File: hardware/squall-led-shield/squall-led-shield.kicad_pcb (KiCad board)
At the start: 2 copper layers, 25.4 x 21 mm, 10 parts, among them J1 SQUALL_HEADER, Q1 Q_2NMOS

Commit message: WIP: Okay, the router is cool once you get it
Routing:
- net Net-(J1-Pad16): track 0.00 -> 7.65 mm, vias 0 -> 1
- net Net-(J1-Pad14): track 0.00 -> 7.39 mm, vias 0 -> 1
- net Net-(J1-Pad18): track 0.00 -> 4.70 mm, vias 0 -> 1
- net Net-(J1-Pad19): track 0.00 -> 4.39 mm, vias 0 -> 1
- net Net-(J1-Pad12): track 0.00 -> 4.33 mm, vias 0 -> 1
- net Net-(J1-Pad20): track 0.00 -> 3.77 mm, vias 0 -> 1
- net Net-(J1-Pad13): track 0.00 -> 3.43 mm, vias 0 -> 1
- net Net-(J1-Pad11): track 0.00 -> 3.04 mm, vias 0 -> 1
- net Net-(J1-Pad15): track 0.00 -> 2.96 mm, vias 0 -> 1
- net Net-(J1-Pad17): track 0.00 -> 2.52 mm, vias 0 -> 1
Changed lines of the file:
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@@
     (thickness 1.6)
     (drawings 3)
-    (tracks 70)
+    (tracks 150)
     (zones 0)
     (modules 10)
@@
   (via (at 145.288 100.457) (size 0.8128) (drill 0.4064) (layers F.Cu B.Cu) (net 12))
   (segment (start 144.23 99.46) (end 144.799 99.46) (width 0.2032) (layer F.Cu) (net 12))
+  (segment (start 161.390368 102.472047) (end 161.390368 103.052832) (width 0.2032) (layer B.Cu) (net 13))
+  (segment (start 161.390368 103.052832) (end 161.1032 103.34) (width 0.2032) (layer B.Cu) (net 13))
+  (segment (start 161.1032 103.34) (end 160.57 103.34) (width 0.2032) (layer B.Cu) (net 13))
+  (segment (start 160.57 103.34) (end 161.1032 103.34) (width 0.2032) (layer F.Cu) (net 13))
+  (segment (start 161.1032 103.34) (end 161.390368 103.052832) (width 0.2032) (layer F.Cu) (net 13))
+  (segment (start 161.390368 103.052832) (end 161.390368 102.472047) (width 0.2032) (layer F.Cu) (net 13))
+  (via (at 161.390368 102.472047) (size 0.8128) (drill 0.4064) (layers F.Cu B.Cu) (net 13))
+  (segment (start 163.28 103.34) (end 163.767202 103.34) (width 0.2032) (layer B.Cu) (net 14))
+  (segment (start 163.522198 102.181198) (end 163.195 102.181198) (width 0.2032) (layer B.Cu) (net 14))
+  (segment (start 163.767202 103.34) (end 163.864001 103.243201) (width 0.2032) (layer B.Cu) (net 14))
+  (segment (start 163.864001 103.243201) (end 163.864001 102.523001) (width 0.2032) (layer B.Cu) (net 14))
+  (segment (start 163.864001 102.523001) (end 163.522198 102.181198) (width 0.2032) (layer B.Cu) (net 14))
+  (segment (start 163.28 103.34) (end 163.8132 103.34) (width 0.2032) (layer F.Cu) (net 14))
+  (segment (start 163.8132 103.34) (end 163.864001 103.289199) (width 0.2032) (layer F.Cu) (net 14))
+  (segment (start 163.864001 103.289199) (end 163.864001 102.536799) (width 0.2032) (layer F.Cu) (net 14))
+  (segment (start 163.864001 102.536799) (end 163.5084 102.181198) (width 0.2032) (layer F.Cu) (net 14))
+  (segment (start 163.5084 102.181198) (end 163.195 102.181198) (width 0.2032) (layer F.Cu) (net 14))
+  (via (at 163.195 102.181198) (size 0.8128) (drill 0.4064) (layers F.Cu B.Cu) (net 14))
+  (segment (start 162.052 103.174797) (end 161.486797 103.74) (width 0.2032) (layer F.Cu) (net 15))
+  (segment (start 161.486797 103.74) (end 160.57 103.74) (width 0.2032) (layer F.Cu) (net 15))
+  (segment (start 160.57 103.74) (end 161.486797 103.74) (width 0.2032) (layer B.Cu) (net 15))
+  (segment (start 161.486797 103.74) (end 162.052 103.174797) (width 0.2032) (layer B.Cu) (net 15))
+  (via (at 162.052 103.174797) (size 0.8128) (drill 0.4064) (layers F.Cu B.Cu) (net 15))
+  (segment (start 163.195 101.215995) (end 164.21961 102.240605) (width 0.2032) (layer F.Cu) (net 16))
+  (segment (start 164.21961 102.240605) (end 164.21961 103.436498) (width 0.2032) (layer F.Cu) (net 16))
+  (segment (start 164.21961 103.436498) (end 163.916108 103.74) (width 0.2032) (layer F.Cu) (net 16))
+  (segment (start 163.916108 103.74) (end 163.8132 103.74) (width 0.2032) (layer F.Cu) (net 16))
+  (segment (start 163.8132 103.74) (end 163.28 103.74) (width 0.2032) (layer F.Cu) (net 16))
+  (segment (start 163.28 103.74) (end 163.87011 103.74) (width 0.2032) (layer B.Cu) (net 16))
+  (segment (start 163.87011 103.74) (end 164.219611 103.390499) (width 0.2032) (layer B.Cu) (net 16))
+  (segment (start 164.219611 103.390499) (end 164.219611 102.240606) (width 0.2032) (layer B.Cu) (net 16))
+  (segment (start 164.219611 102.240606) (end 163.195 101.215995) (width 0.2032) (layer B.Cu) (net 16))
+  (via (at 163.195 101.215995) (size 0.8128) (drill 0.4064) (layers F.Cu B.Cu) (net 16))
+  (segment (start 162.052 104.14) (end 160.57 104.14) (width 0.2032) (layer B.Cu) (net 17))
+  (segment (start 160.57 104.14) (end 162.052 104.14) (width 0.2032) (layer F.Cu) (net 17))
+  (via (at 162.052 104.14) (size 0.8128) (drill 0.4064) (layers F.Cu B.Cu) (net 17))
+  (segment (start 164.298476 101.385524) (end 164.575221 101.662269) (width 0.2032) (layer B.Cu) (net 18))
+  (segment (start 164.575221 101.662269) (end 164.575221 103.537797) (width 0.2032) (layer B.Cu) (net 18))
+  (segment (start 164.575221 103.537797) (end 164.004017 104.109001) (width 0.2032) (layer B.Cu) (net 18))
+  (segment (start 164.004017 104.109001) (end 163.310999 104.109001) (width 0.2032) (layer B.Cu) (net 18))
+  (segment (start 163.310999 104.109001) (end 163.28 104.14) (width 0.2032) (layer B.Cu) (net 18))
+  (segment (start 163.28 104.14) (end 164.019016 104.14) (width 0.2032) (layer F.Cu) (net 18))
+  (segment (start 164.019016 104.14) (end 164.57522 103.583796) (width 0.2032) (layer F.Cu) (net 18))
+  (segment (start 164.57522 103.583796) (end 164.57522 101.662268) (width 0.2032) (layer F.Cu) (net 18))
+  (segment (start 164.57522 101.662268) (end 164.298476 101.385524) (width 0.2032) (layer F.Cu) (net 18))
+  (via (at 164.298476 101.385524) (size 0.8128) (drill 0.4064) (layers F.Cu B.Cu) (net 18))
+  (segment (start 161.454603 105.123367) (end 161.454603 104.891403) (width 0.2032) (layer B.Cu) (net 19))
+  (segment (start 161.454603 104.891403) (end 161.1032 104.54) (width 0.2032) (layer B.Cu) (net 19))
+  (segment (start 161.1032 104.54) (end 160.57 104.54) (width 0.2032) (layer B.Cu) (net 19))
+  (segment (start 160.57 104.54) (end 161.1032 104.54) (width 0.2032) (layer F.Cu) (net 19))
+  (segment (start 161.1032 104.54) (end 161.454603 104.891403) (width 0.2032) (layer F.Cu) (net 19))
+  (segment (start 161.454603 104.891403) (end 161.454603 105.123367) (width 0.2032) (layer F.Cu) (net 19))
+  (via (at 161.454603 105.123367) (size 0.8128) (drill 0.4064) (layers F.Cu B.Cu) (net 19))
+  (segment (start 162.306 106.172) (end 162.306 104.9808) (width 0.2032) (layer B.Cu) (net 20))
+  (segment (start 162.306 104.9808) (end 162.7468 104.54) (width 0.2032) (layer B.Cu) (net 20))
+  (segment (start 162.7468 104.54) (end 163.28 104.54) (width 0.2032) (layer B.Cu) (net 20))
+  (segment (start 163.28 104.54) (end 162.7468 104.54) (width 0.2032) (layer F.Cu) (net 20))
+  (segment (start 162.7468 104.54) (end 162.306 104.9808) (width 0.2032) (layer F.Cu) (net 20))
+  (segment (start 162.306 104.9808) (end 162.306 106.172) (width 0.2032) (layer F.Cu) (net 20))
+  (via (at 162.306 106.172) (size 0.8128) (drill 0.4064) (layers F.Cu B.Cu) (net 20))
+  (segment (start 160.57 104.94) (end 160.082798 104.94) (width 0.2032) (layer F.Cu) (net 21))
+  (segment (start 160.082798 104.94) (end 159.985999 105.036799) (width 0.2032) (layer F.Cu) (net 21))
+  (segment (start 159.985999 105.036799) (end 159.985999 105.756999) (width 0.2032) (layer F.Cu) (net 21))
+  (segment (start 159.985999 105.756999) (end 160.401 106.172) (width 0.2032) (layer F.Cu) (net 21))
+  (segment (start 160.401 106.172) (end 160.655 106.172) (width 0.2032) (layer F.Cu) (net 21))
+  (segment (start 160.57 104.94) (end 160.0368 104.94) (width 0.2032) (layer B.Cu) (net 21))
+  (segment (start 160.0368 104.94) (end 159.985999 104.990801) (width 0.2032) (layer B.Cu) (net 21))
+  (segment (start 159.985999 104.990801) (end 159.985999 105.743201) (width 0.2032) (layer B.Cu) (net 21))
+  (segment (start 159.985999 105.743201) (end 160.414798 106.172) (width 0.2032) (layer B.Cu) (net 21))
+  (segment (start 160.414798 106.172) (end 160.655 106.172) (width 0.2032) (layer B.Cu) (net 21))
+  (via (at 160.655 106.172) (size 0.8128) (drill 0.4064) (layers F.Cu B.Cu) (net 21))
+  (segment (start 163.449 106.098802) (end 163.864001 105.683801) (width 0.2032) (layer F.Cu) (net 22))
+  (segment (start 163.864001 105.683801) (end 163.864001 104.990801) (width 0.2032) (layer F.Cu) (net 22))
+  (segment (start 163.864001 104.990801) (end 163.8132 104.94) (width 0.2032) (layer F.Cu) (net 22))
+  (segment (start 163.8132 104.94) (end 163.28 104.94) (width 0.2032) (layer F.Cu) (net 22))
+  (segment (start 163.28 104.94) (end 163.8132 104.94) (width 0.2032) (layer B.Cu) (net 22))
+  (segment (start 163.8132 104.94) (end 163.864001 104.990801) (width 0.2032) (layer B.Cu) (net 22))
+  (segment (start 163.864001 104.990801) (end 163.864001 105.683801) (width 0.2032) (layer B.Cu) (net 22))
+  (segment (start 163.864001 105.683801) (end 163.449 106.098802) (width 0.2032) (layer B.Cu) (net 22))
+  (via (at 163.449 106.098802) (size 0.8128) (drill 0.4064) (layers F.Cu B.Cu) (net 22))
   (segment (start 151.468 94.912) (end 151.743 94.637) (width 0.2032) (layer F.Cu) (net 23))
   (segment (start 151.743 94.637) (end 153.67 94.637) (width 0.2032) (layer F.Cu) (net 23))

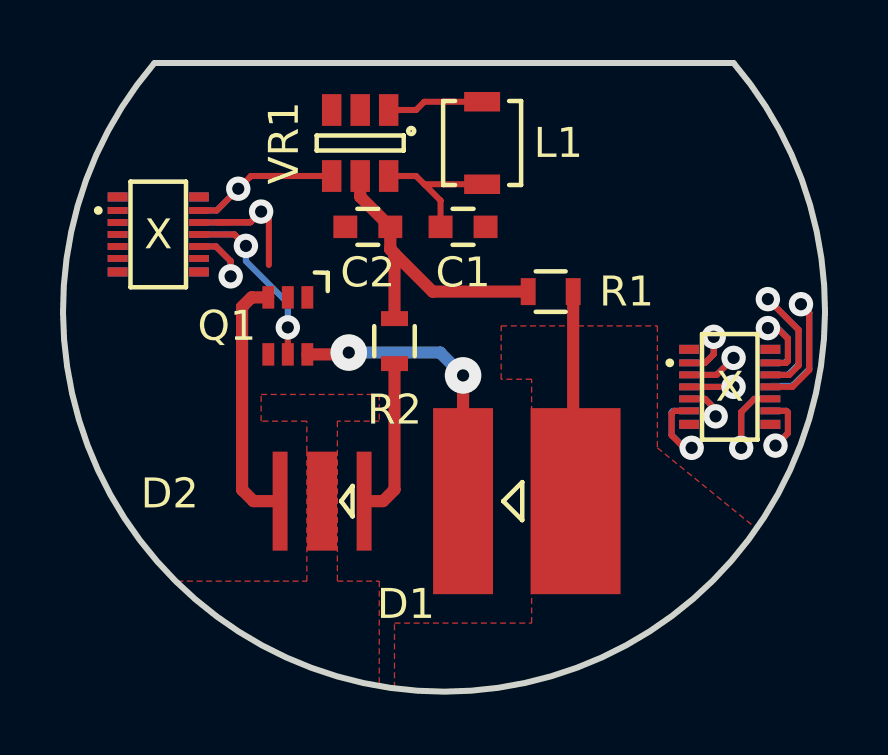
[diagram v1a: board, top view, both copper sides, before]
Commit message: WIP: Tie regulator to VCC
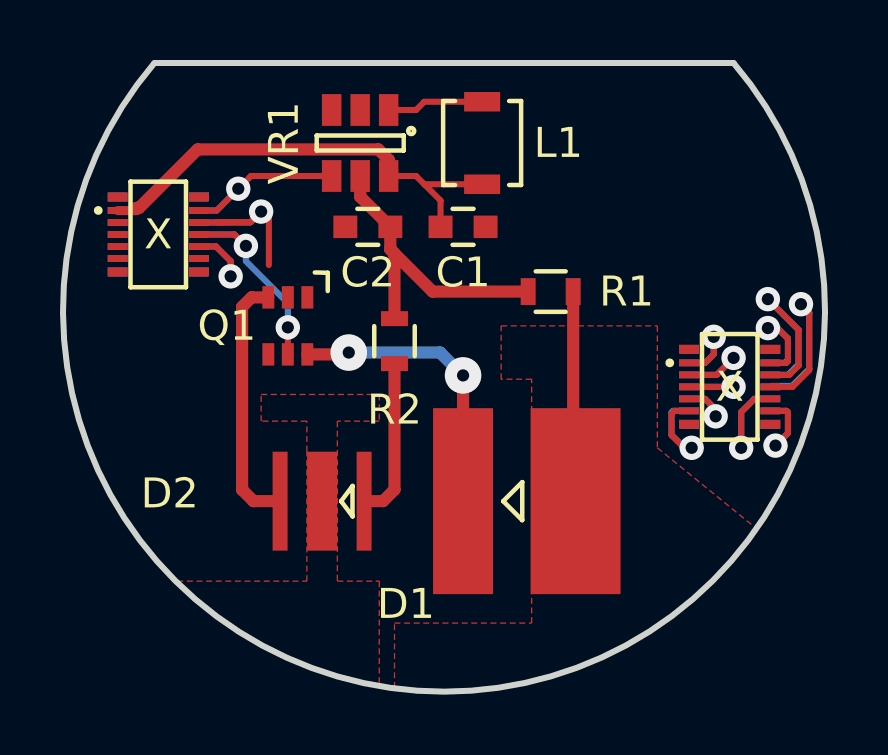
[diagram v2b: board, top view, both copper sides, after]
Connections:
- C1 pad 1: Net-(C1-Pad1) -> VCC
- L1 pad 1: Net-(C1-Pad1) -> VCC
- VR1 pad 6: Net-(C1-Pad1) -> VCC
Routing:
- net VCC: track 0.00 -> 16.3 mm
- net Net-(C1-Pad1): track 4.98 -> 0.00 mm

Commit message: Okay. That may be a board. Finally.
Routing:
- net GND: track 0.00 -> 13.5 mm, vias 0 -> 7
- net /CREE_THERMAL: track 0.00 -> 9.54 mm, vias 0 -> 3
- net Net-(D1-Pad2): track 7.02 -> 16.5 mm, vias 0 -> 3
- net /LED_IR: track 7.31 -> 8.65 mm
- added copper zone on B.Cu, net /CREE_THERMAL
- added copper zone on B.Cu, net GND
- added copper zone on F.Cu, net GND
- added copper zone on B.Cu, net Net-(D1-Pad2)

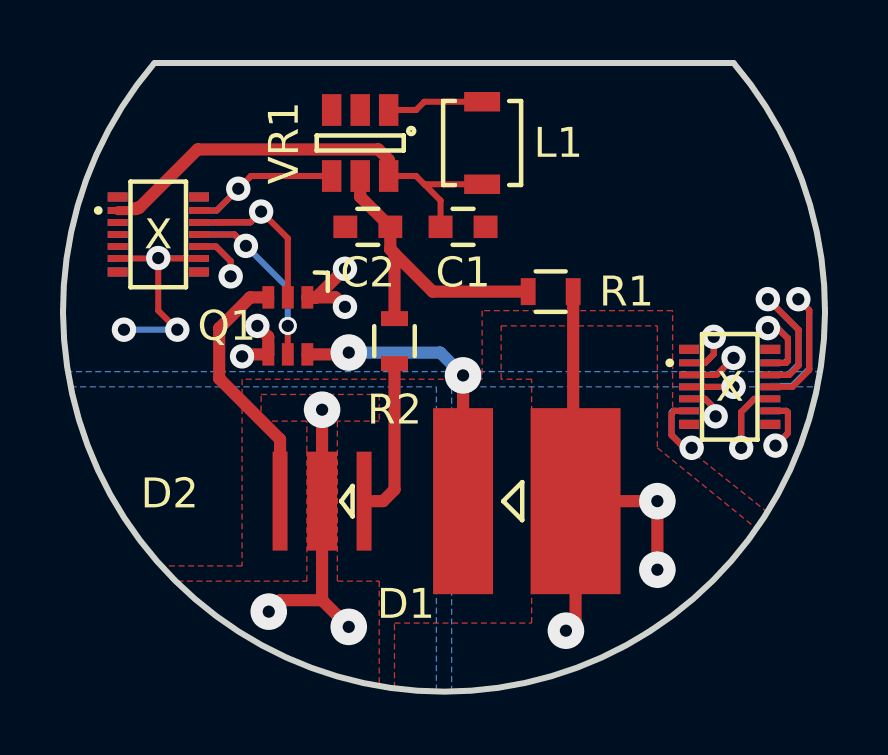
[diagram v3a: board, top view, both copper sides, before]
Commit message: Clean up silkscreen
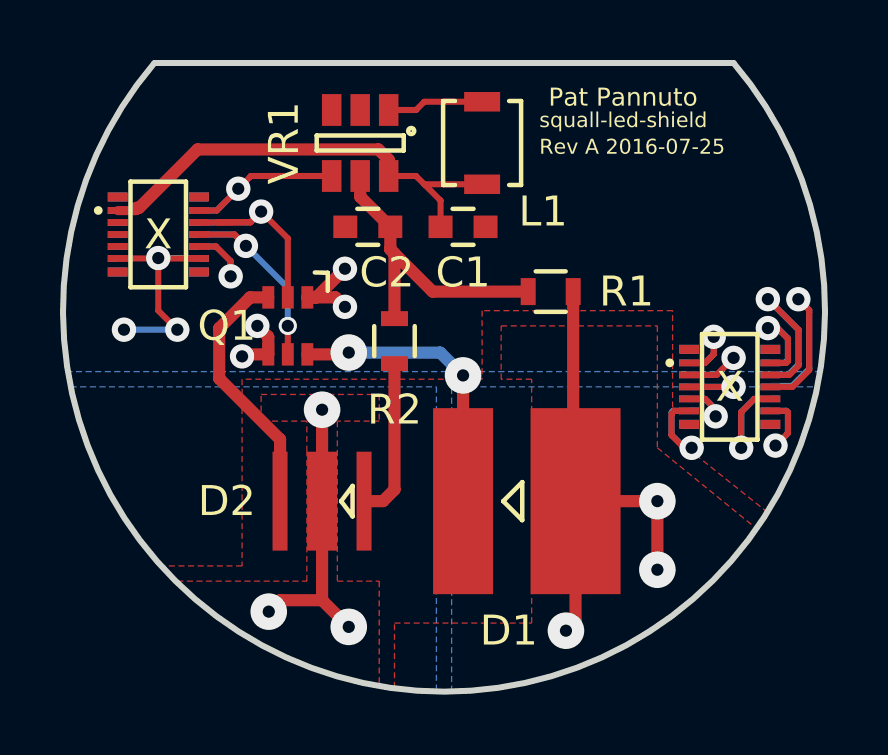
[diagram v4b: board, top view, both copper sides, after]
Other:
- board text added: "Pat Pannuto"
- board text added: "Rev A 2016-07-25"
- board text added: "squall-led-shield"
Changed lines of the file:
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@@
   (general
     (links 41)
-    (no_connects 7)
+    (no_connects 11)
     (area 137.2318 92.590943 282.218715 163.828)
     (thickness 1.6)
-    (drawings 3)
+    (drawings 6)
     (tracks 199)
     (zones 0)
@@
     (uvia_min_drill 0.1524)
     (pcb_text_width 0.3)
-    (pcb_text_size 1.5 1.5)
+    (pcb_text_size 1.016 1.016)
     (mod_edge_width 0.15)
     (mod_text_size 1 1)
@@
     (tags "capacitor 0603")
     (attr smd)
-    (fp_text reference C2 (at 0 -1.524 180) (layer F.SilkS)
+    (fp_text reference C2 (at -0.635 -1.524 180) (layer F.SilkS)
       (effects (font (size 1 1) (thickness 0.15)))
     )
@@
   (module Squall:INDUCTOR_VLF (layer F.Cu)
     (at 153.67 96.012 90)
-    (fp_text reference L1 (at 0 2.54 180) (layer F.SilkS)
+    (fp_text reference L1 (at -2.286 2.032 180) (layer F.SilkS)
       (effects (font (size 1 1) (thickness 0.15)))
     )
@@
   (module Squall:CREE_XT-E (layer F.Cu)
     (at 148.336 107.95 180)
-    (fp_text reference D2 (at 5.08 0.254 180) (layer F.SilkS)
+    (fp_text reference D2 (at 3.175 0 180) (layer F.SilkS)
       (effects (font (size 1 1) (thickness 0.15)))
     )
@@
   (module Squall:VSMY785X (layer F.Cu)
     (at 155.135 107.95 90)
-    (fp_text reference D1 (at -3.429 -4.005 180) (layer F.SilkS)
+    (fp_text reference D1 (at -4.318 -0.576 180) (layer F.SilkS)
       (effects (font (size 1 1) (thickness 0.15)))
     )
@@
     (pad 2 smd rect (at 0 1.65 90) (size 6.2 3) (layers F.Cu F.Paste F.Mask)
       (net 4 "Net-(D1-Pad2)"))
+  )
+  (gr_text "Rev A 2016-07-25" (at 155.575 96.139) (layer F.SilkS)
+    (effects (font (size 0.5 0.5) (thickness 0.05)) (justify left))
+  )
+  (gr_text squall-led-shield (at 155.575 95.25) (layer F.SilkS)
+    (effects (font (size 0.5 0.5) (thickness 0.05)) (justify left))
+  )
+  (gr_text "Pat Pannuto" (at 158.369 94.488) (layer F.SilkS)
+    (effects (font (size 0.6 0.6) (thickness 0.05)))
   )
   (gr_line (start 142.748 93.345) (end 162.052 93.345) (layer Edge.Cuts) (width 0.2))
@@
     (connect_pads yes (clearance 0.2032))
     (min_thickness 0.2032)
-    (fill yes (arc_segments 32) (thermal_gap 0.508) (thermal_bridge_width 0.508))
+    (fill (arc_segments 32) (thermal_gap 0.508) (thermal_bridge_width 0.508))
     (polygon
       (pts
@@
     (connect_pads yes (clearance 0.2032))
     (min_thickness 0.2032)
-    (fill yes (arc_segments 32) (thermal_gap 0.508) (thermal_bridge_width 0.508))
+    (fill (arc_segments 32) (thermal_gap 0.508) (thermal_bridge_width 0.508))
     (polygon
       (pts
@@
     (connect_pads (clearance 0.2032))
     (min_thickness 0.2032)
-    (fill yes (arc_segments 16) (thermal_gap 0.508) (thermal_bridge_width 0.508))
+    (fill (arc_segments 16) (thermal_gap 0.508) (thermal_bridge_width 0.508))
     (polygon
       (pts
@@
     (connect_pads (clearance 0.2032))
     (min_thickness 0.254)
-    (fill yes (arc_segments 16) (thermal_gap 0.508) (thermal_bridge_width 0.508))
+    (fill (arc_segments 16) (thermal_gap 0.508) (thermal_bridge_width 0.508))
     (polygon
       (pts
@@
     (connect_pads (clearance 0.2032))
     (min_thickness 0.2032)
-    (fill yes (arc_segments 16) (thermal_gap 0.508) (thermal_bridge_width 0.508))
+    (fill (arc_segments 16) (thermal_gap 0.508) (thermal_bridge_width 0.508))
     (polygon
       (pts
@@
     (connect_pads (clearance 0.2032))
     (min_thickness 0.2032)
-    (fill yes (arc_segments 16) (thermal_gap 0.508) (thermal_bridge_width 0.508))
+    (fill (arc_segments 16) (thermal_gap 0.508) (thermal_bridge_width 0.508))
     (polygon
       (pts

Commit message: Add CubeWorks logo
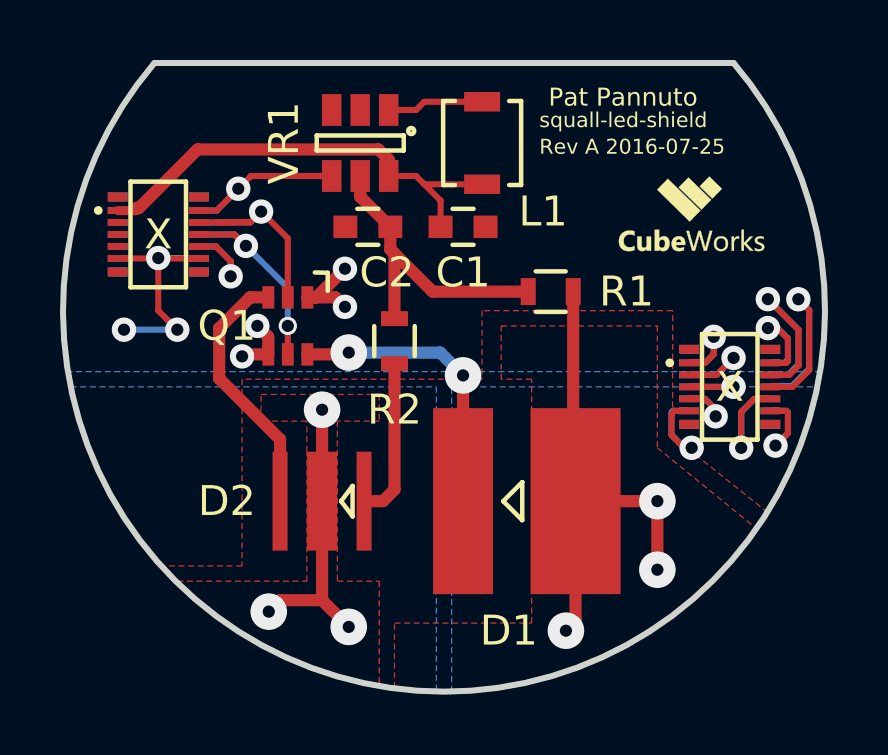
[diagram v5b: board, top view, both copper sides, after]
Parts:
- added _1: CubeWorks-Logo, Squall:CubeWorks_Logo-5mm, F.Cu at (160.7, 98.4)
